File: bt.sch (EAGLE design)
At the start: 16 parts, among them Q1 MOSFET-NCHANNELSMD, Q2 MOSFET-NCHANNELSMD

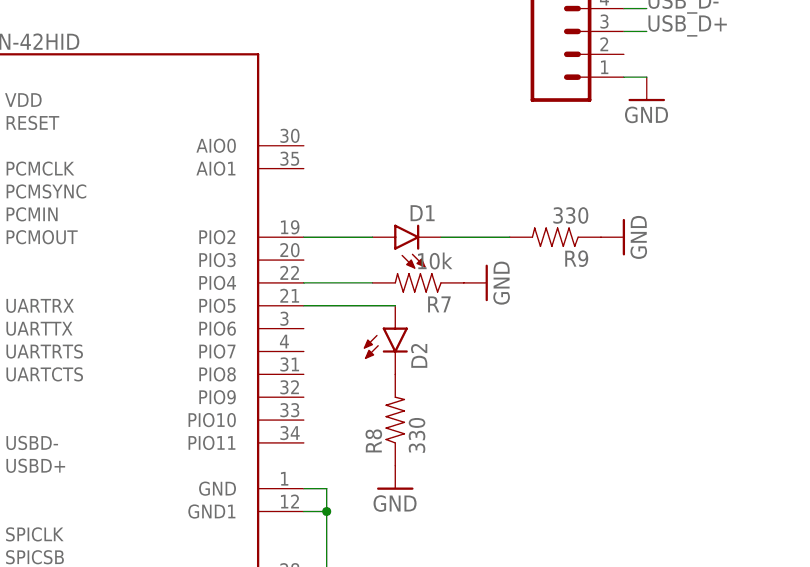
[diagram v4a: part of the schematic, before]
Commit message: Got a good handle on the bt module so went ahead and ordered one
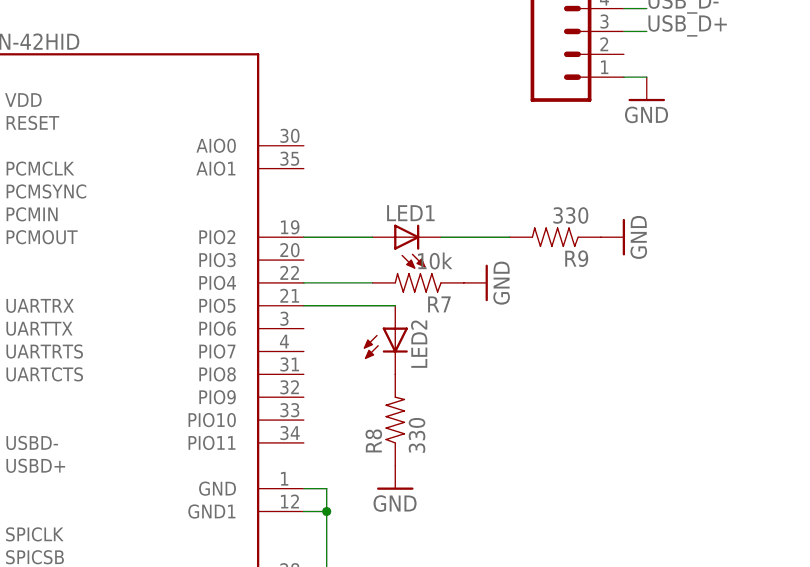
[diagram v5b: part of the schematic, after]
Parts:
- removed D1, D2: (no value), SparkFun-LED:LED1206
- added LED1, LED2: (no value), adafruit:LEDCHIP-LED0805
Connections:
- net N$1: now also LED2.C; no longer D2.C
- net N$10: now also LED2.A; no longer D2.A
- net N$3: now also LED1.C; no longer D1.C
- net N$8: now also LED1.A; no longer D1.A
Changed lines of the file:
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@@
 <?xml version="1.0" encoding="utf-8"?>
 <!DOCTYPE eagle SYSTEM "eagle.dtd">
-<eagle version="6.6.0">
+<eagle version="7.4.0">
 <drawing>
 <settings>
@@
 <layer number="230" name="230bmp" color="7" fill="1" visible="yes" active="yes"/>
 <layer number="231" name="231bmp" color="7" fill="1" visible="yes" active="yes"/>
+<layer number="232" name="Eagle3D_PG2" color="7" fill="1" visible="no" active="no"/>
+<layer number="233" name="Eagle3D_PG3" color="7" fill="1" visible="no" active="no"/>
 <layer number="248" name="Housing" color="7" fill="1" visible="yes" active="yes"/>
 <layer number="249" name="Edge" color="7" fill="1" visible="yes" active="yes"/>
@@
 <part name="R9" library="SparkFun-Resistors" deviceset="0.22OHM-1/4W-1%(0805)" device="" value="330"/>
 <part name="GND4" library="SparkFun" deviceset="GND" device=""/>
-<part name="D1" library="SparkFun-LED" deviceset="LED" device="1206"/>
-<part name="D2" library="SparkFun-LED" deviceset="LED" device="1206"/>
 <part name="GND5" library="SparkFun" deviceset="GND" device=""/>
 <part name="GND6" library="SparkFun" deviceset="GND" device=""/>
@@
 <part name="USB" library="mine" deviceset="M06" device="SMD-FEMALE-V2-NOSILK"/>
 <part name="RN-42HID" library="mine" deviceset="BLUETOOTH-RN42-NOSILK" device="&quot;"/>
+<part name="LED1" library="adafruit" deviceset="LED" device="CHIP-LED0805"/>
+<part name="LED2" library="adafruit" deviceset="LED" device="CHIP-LED0805"/>
 </parts>
 <sheets>
@@
 <instance part="R9" gate="G$1" x="76.2" y="48.26" rot="R180"/>
 <instance part="GND4" gate="1" x="68.58" y="43.18" rot="R90"/>
-<instance part="D1" gate="G$1" x="58.42" y="48.26" rot="R90"/>
-<instance part="D2" gate="G$1" x="58.42" y="38.1"/>
 <instance part="GND5" gate="1" x="83.82" y="48.26" rot="R90"/>
 <instance part="GND6" gate="1" x="58.42" y="20.32"/>
@@
 <instance part="USB" gate="G$1" x="78.74" y="71.12"/>
 <instance part="RN-42HID" gate="G$1" x="27.94" y="35.56"/>
+<instance part="LED1" gate="G$1" x="58.42" y="48.26" rot="R90"/>
+<instance part="LED2" gate="G$1" x="58.42" y="38.1"/>
 </instances>
 <busses>
@@
 <segment>
 <wire x1="48.26" y1="48.26" x2="55.88" y2="48.26" width="0.1524" layer="91"/>
-<pinref part="D1" gate="G$1" pin="A"/>
 <pinref part="RN-42HID" gate="G$1" pin="PIO2"/>
+<pinref part="LED1" gate="G$1" pin="A"/>
 </segment>
 </net>
@@
 <segment>
 <wire x1="48.26" y1="40.64" x2="58.42" y2="40.64" width="0.1524" layer="91"/>
-<pinref part="D2" gate="G$1" pin="A"/>
 <pinref part="RN-42HID" gate="G$1" pin="PIO5"/>
+<pinref part="LED2" gate="G$1" pin="A"/>
 </segment>
 </net>
@@
 </segment>
 </net>
-<net name="N$1" class="0">
-<segment>
-<pinref part="D2" gate="G$1" pin="C"/>
-<pinref part="R8" gate="G$1" pin="2"/>
-</segment>
-</net>
 <net name="N$3" class="0">
 <segment>
-<pinref part="D1" gate="G$1" pin="C"/>
 <pinref part="R9" gate="G$1" pin="2"/>
 <wire x1="71.12" y1="48.26" x2="63.5" y2="48.26" width="0.1524" layer="91"/>
-</segment>
-</net>
+<pinref part="LED1" gate="G$1" pin="C"/>
+</segment>
+</net>
+<net name="N$1" class="0">
+<segment>
+<pinref part="R8" gate="G$1" pin="2"/>
+<pinref part="LED2" gate="G$1" pin="C"/>
+</segment>
+</net>
